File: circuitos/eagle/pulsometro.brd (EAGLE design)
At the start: 83.5 x 69.2 mm, 33 parts, among them IC1 TLV2472, IC2 TLV2472, IC3 PIC18F2550_28DIP, X1 20MHz

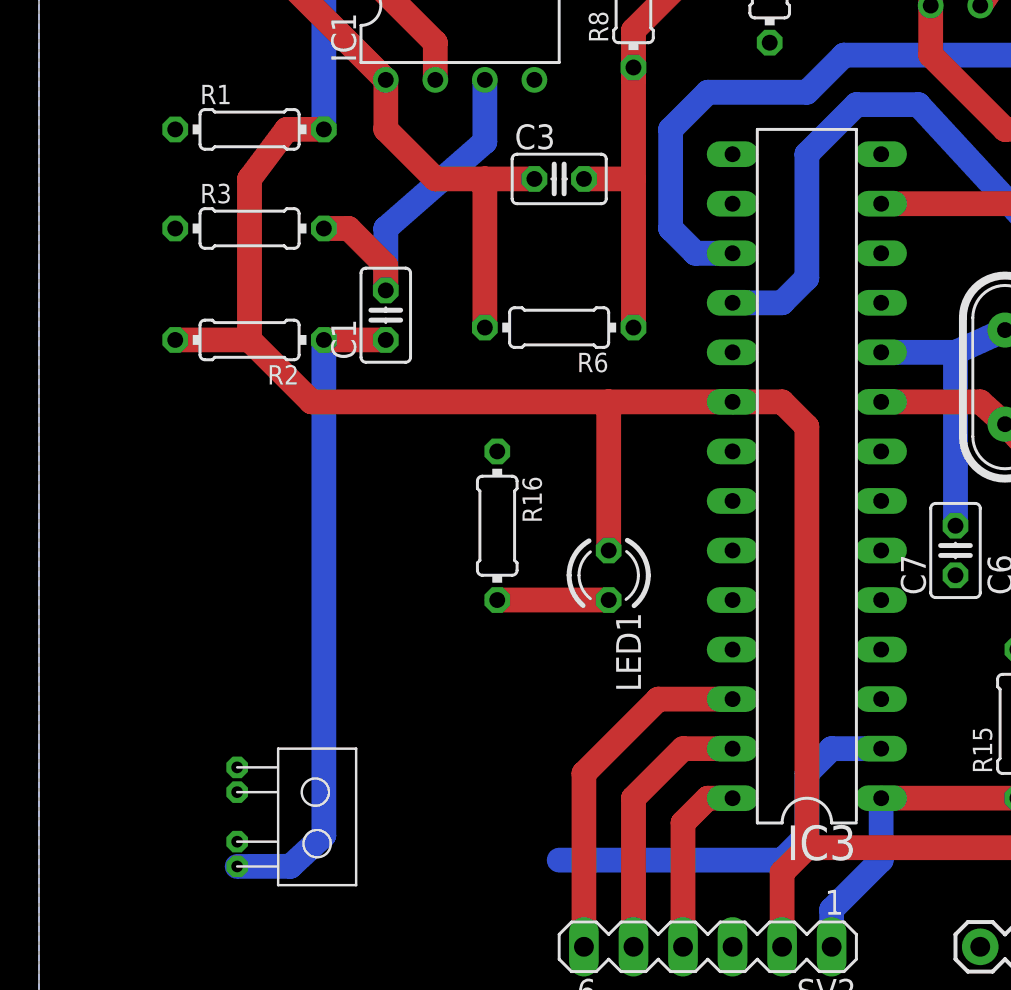
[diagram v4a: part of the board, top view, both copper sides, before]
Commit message: Include pcb in report
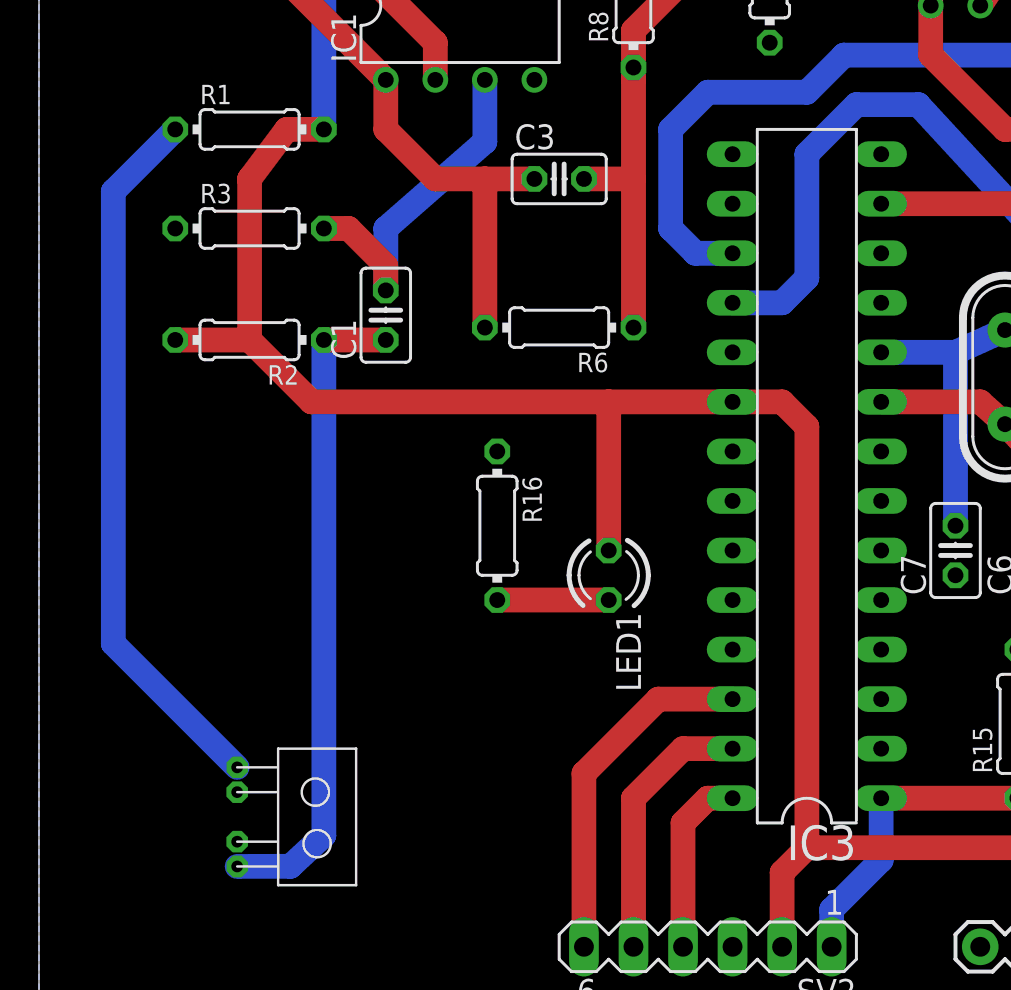
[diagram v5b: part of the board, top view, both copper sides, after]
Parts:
- IC3: value PIC18F2550_28DIP -> PIC18LF2553_28DIP
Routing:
- net N$1: track 0.00 -> 36.7 mm
- net RA0: track 20.7 -> 0.00 mm
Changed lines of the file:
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@@
 <layer number="113" name="IDFDebug" color="4" fill="1" visible="no" active="yes"/>
 <layer number="116" name="Patch_BOT" color="9" fill="4" visible="no" active="yes"/>
-<layer number="118" name="Rect_Pads" color="7" fill="1" visible="yes" active="yes"/>
+<layer number="118" name="Rect_Pads" color="7" fill="1" visible="no" active="yes"/>
 <layer number="121" name="_tsilk" color="7" fill="1" visible="no" active="yes"/>
 <layer number="122" name="_bsilk" color="7" fill="1" visible="no" active="yes"/>
@@
 <element name="IC1" library="linear" package="DIL08" value="TLV2472" x="36.83" y="64.77"/>
 <element name="IC2" library="linear" package="DIL08" value="TLV2472" x="64.77" y="68.58" rot="R180"/>
-<element name="IC3" library="microchip" package="DIL28-3" value="PIC18F2550_28DIP" x="54.61" y="40.64" rot="R90">
+<element name="IC3" library="microchip" package="DIL28-3" value="PIC18LF2553_28DIP" x="54.61" y="40.64" rot="R90">
 <attribute name="OC_NEWARK" value="80K6054" x="54.61" y="40.64" size="1.778" layer="27" rot="R90" display="off"/>
 <attribute name="MPN" value="PIC18F2550-I/SP" x="54.61" y="40.64" size="1.778" layer="27" rot="R90" display="off"/>
@@
 <signal name="RA0">
 <contactref element="IC3" pad="2"/>
-<wire x1="41.91" y1="20.955" x2="53.34" y2="20.955" width="1.27" layer="16"/>
-<wire x1="53.34" y1="20.955" x2="54.61" y2="22.225" width="1.27" layer="16"/>
-<wire x1="54.61" y1="22.225" x2="54.61" y2="25.4" width="1.27" layer="16"/>
-<wire x1="54.61" y1="25.4" x2="55.88" y2="26.67" width="1.27" layer="16"/>
-<wire x1="55.88" y1="26.67" x2="58.42" y2="26.67" width="1.27" layer="16"/>
 </signal>
 <signal name="N$8">
@@
 <contactref element="U$1" pad="PIN_1"/>
 <contactref element="R1" pad="1"/>
-<wire x1="25.4" y1="25.71" x2="22.225" y2="58.42" width="0" layer="19" extent="1-1"/>
+<wire x1="25.4" y1="25.71" x2="19.05" y2="32.06" width="1.27" layer="16"/>
+<wire x1="19.05" y1="32.06" x2="19.05" y2="55.245" width="1.27" layer="16"/>
+<wire x1="19.05" y1="55.245" x2="22.225" y2="58.42" width="1.27" layer="16"/>
 </signal>
 </signals>
